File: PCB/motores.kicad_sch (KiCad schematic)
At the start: 30 parts, among them IC2 IR2175STRPBF, J10 Conn_01x03, J11 Conn_01x03, J12 motor_dc, J9 motor_lineal, K1 G6E, K2 G6E, K3 G6E, K4 G6E, Q1 AO3401A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

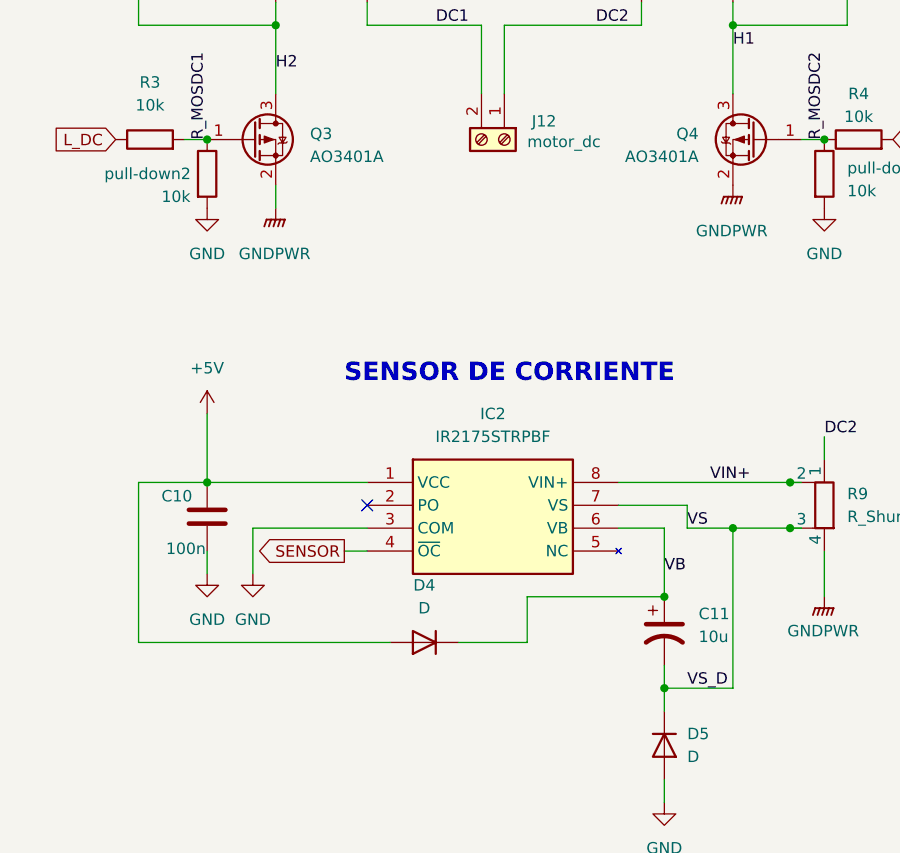
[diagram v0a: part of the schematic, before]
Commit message: Fixed labels and ERC errors
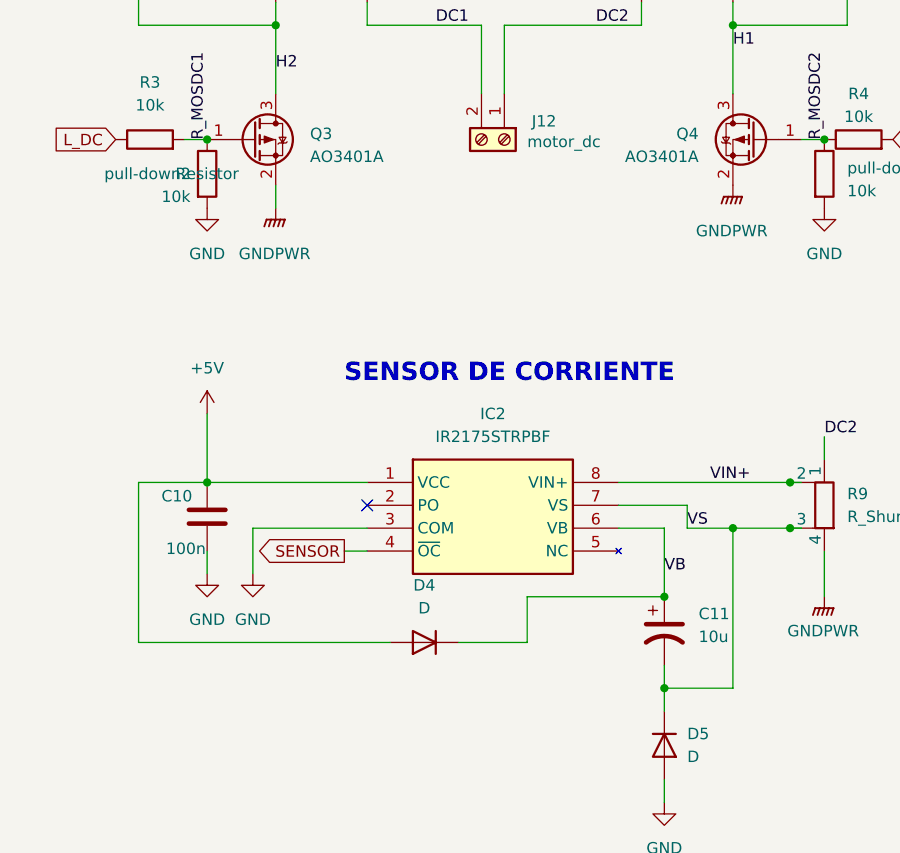
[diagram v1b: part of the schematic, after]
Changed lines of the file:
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@@
 	(wire
 		(pts
-			(xy 175.26 124.46) (xy 193.04 124.46)
-		)
-		(stroke
-			(width 0)
-			(type default)
-		)
-	)
-	(wire
-		(pts
 			(xy 50.8 60.96) (xy 63.5 60.96)
 		)
@@
 	(wire
 		(pts
+			(xy 175.26 124.46) (xy 193.04 124.46)
+		)
+		(stroke
+			(width 0)
+			(type default)
+		)
+	)
+	(wire
+		(pts
 			(xy 208.28 73.66) (xy 208.28 81.28)
 		)
@@
 		)
 	)
-	(label "VS_D"
-		(at 228.6 147.32 0)
-		(effects
-			(font
-				(size 1.27 1.27)
-			)
-			(justify left bottom)
-		)
-	)
 	(global_label "L_DC"
 		(shape input)
@@
 	)
 	(symbol
-		(lib_name "GND_1")
 		(lib_id "power:GND")
 		(at 66.04 142.24 0)
@@
 			)
 		)
-		(property "Description" ""
+		(property "Description" "-4.0A Id, -30V Vds, P-Channel MOSFET, SOT-23"
 			(at 236.22 86.36 0)
 			(effects
@@
 					(size 1.27 1.27)
 				)
+				(hide yes)
 			)
 		)
@@
 			)
 		)
-		(property "Description" ""
+		(property "Description" "Omron Subminiature Sensitive SPDT Signal Switching Relay, Single-Side Stable"
 			(at 109.22 73.66 0)
 			(effects
@@
 					(size 1.27 1.27)
 				)
+				(hide yes)
 			)
 		)
@@
 			)
 		)
-		(property "Description" ""
+		(property "Description" "Omron Subminiature Sensitive SPDT Signal Switching Relay, Single-Side Stable"
 			(at 68.58 73.66 0)
 			(effects
@@
 					(size 1.27 1.27)
 				)
+				(hide yes)
 			)
 		)
@@
 			)
 		)
-		(property "Description" ""
+		(property "Description" "Power symbol creates a global label with name \"GNDPWR\" , global ground"
 			(at 114.3 99.06 0)
 			(effects
@@
 					(size 1.27 1.27)
 				)
+				(hide yes)
 			)
 		)
@@
 			)
 		)
-		(property "Description" ""
+		(property "Description" "Resistor"
 			(at 49.53 91.44 0)
 			(effects
@@
 					(size 1.27 1.27)
 				)
+				(hide yes)
 			)
 		)
@@
 			)
 		)
-		(property "Description" ""
+		(property "Description" "Power symbol creates a global label with name \"GND\" , ground"
 			(at 121.92 101.6 0)
 			(effects
@@
 					(size 1.27 1.27)
 				)
+				(hide yes)
 			)
 		)
@@
 	)
 	(symbol
-		(lib_name "GNDPWR_1")
 		(lib_id "power:GNDPWR")
 		(at 243.84 137.16 0)
@@
 	)
 	(symbol
-		(lib_name "+12V_1")
 		(lib_id "power:+12V")
 		(at 88.9 58.42 0)
@@
 			)
 		)
-		(property "Description" ""
-			(at 63.5 99.06 0)
+		(property "Description" "Power symbol creates a global label with name \"GNDPWR\" , global ground"
+			(at 20.32 99.06 0)
 			(effects
 				(font
 					(size 1.27 1.27)
 				)
+				(hide yes)
 			)
 		)
@@
 			)
 		)
-		(property "Description" ""
+		(property "Description" "Resistor"
 			(at 121.92 97.79 0)
 			(effects
@@
 					(size 1.27 1.27)
 				)
+				(hide yes)
 			)
 		)
@@
 			)
 		)
-		(property "Description" ""
+		(property "Description" "Power symbol creates a global label with name \"GNDPWR\" , global ground"
 			(at 228.6 50.8 0)
 			(effects
@@
 					(size 1.27 1.27)
 				)
+				(hide yes)
 			)
 		)
@@
 	)
 	(symbol
-		(lib_name "GND_2")
 		(lib_id "power:GND")
 		(at 226.06 160.02 0)
@@
 			)
 		)
-		(property "Description" ""
+		(property "Description" "Resistor"
 			(at 243.84 90.17 0)
 			(effects
@@
 					(size 1.27 1.27)
 				)
+				(hide yes)
 			)
 		)
@@
 			)
 		)
-		(property "Description" ""
+		(property "Description" "Power symbol creates a global label with name \"+12V\""
 			(at 208.28 45.72 0)
 			(effects
@@
 					(size 1.27 1.27)
 				)
+				(hide yes)
 			)
 		)
@@
 			)
 		)
-		(property "Description" ""
+		(property "Description" "Resistor"
 			(at 175.26 90.17 0)
 			(effects
@@
 			)
 		)
-		(property "Description" ""
+		(property "Description" "Power symbol creates a global label with name \"GNDPWR\" , global ground"
 			(at 233.68 91.44 0)
 			(effects
@@
 					(size 1.27 1.27)
 				)
+				(hide yes)
 			)
 		)
@@
 			)
 		)
-		(property "Description" ""
+		(property "Description" "Power symbol creates a global label with name \"GNDPWR\" , global ground"
 			(at 182.88 93.98 0)
 			(effects
@@
 					(size 1.27 1.27)
 				)
+				(hide yes)
 			)
 		)
@@
 			)
 		)
-		(property "Description" ""
+		(property "Description" "Power symbol creates a global label with name \"GND\" , ground"
 			(at 175.26 93.98 0)
 			(effects
@@
 					(size 1.27 1.27)
 				)
+				(hide yes)
 			)
 		)
@@
 	)
 	(symbol
-		(lib_name "GND_1")
 		(lib_id "power:GND")
 		(at 92.71 142.24 0)
@@
 	)
 	(symbol
-		(lib_name "GND_3")
 		(lib_id "power:GND")
 		(at 175.26 134.62 0)
@@
 			)
 		)
-		(property "Description" ""
+		(property "Description" "Power symbol creates a global label with name \"GND\" , ground"
 			(at 243.84 93.98 0)
 			(effects
@@
 					(size 1.27 1.27)
 				)
+				(hide yes)
 			)
 		)
@@
 			)
 		)
-		(property "Description" ""
+		(property "Description" "Resistor"
 			(at 55.88 95.25 0)
 			(effects
@@
 					(size 1.27 1.27)
 				)
+				(hide yes)
 			)
 		)
@@
 	)
 	(symbol
-		(lib_name "GND_2")
 		(lib_id "power:GND")
 		(at 180.34 134.62 0)
@@
 	)
 	(symbol
-		(lib_name "GNDPWR_2")
 		(lib_id "power:GNDPWR")
 		(at 68.58 63.5 0)
@@
 		(on_board yes)
 		(dnp no)
-		(fields_autoplaced yes)
 		(property "Reference" "Q1"
 			(at 67.31 90.805 0)
@@
 			)
 		)
-		(property "Description" ""
-			(at 60.96 91.44 0)
+		(property "Description" "-4.0A Id, -30V Vds, P-Channel MOSFET, SOT-23"
+			(at 45.72 104.14 0)
 			(effects
 				(font
 					(size 1.27 1.27)
 				)
+				(hide yes)
 			)
 		)
@@
 			)
 		)
-		(property "Description" ""
+		(property "Description" "-4.0A Id, -30V Vds, P-Channel MOSFET, SOT-23"
 			(at 116.84 93.98 0)
 			(effects
@@
 					(size 1.27 1.27)
 				)
+				(hide yes)
 			)
 		)
@@
 			)
 		)
-		(property "Description" ""
+		(property "Description" "Omron Subminiature Sensitive SPDT Signal Switching Relay, Single-Side Stable"
 			(at 187.96 63.5 0)
 			(effects
@@
 					(size 1.27 1.27)
 				)
+				(hide yes)
 			)
 		)
@@
 			)
 		)
-		(property "Description" ""
+		(property "Description" "Power symbol creates a global label with name \"GNDPWR\" , global ground"
 			(at 187.96 48.26 0)
 			(effects
@@
 					(size 1.27 1.27)
 				)
+				(hide yes)
 			)
 		)
@@
 			)
 		)
-		(property "Description" ""
+		(property "Description" "Resistor"
 			(at 128.27 93.98 0)
 			(effects
@@
 					(size 1.27 1.27)
 				)
+				(hide yes)
 			)
 		)
@@
 	)
 	(symbol
-		(lib_name "GNDPWR_2")
 		(lib_id "power:GNDPWR")
 		(at 109.22 63.5 0)
@@
 			)
 		)
-		(property "Description" ""
+		(property "Description" "Omron Subminiature Sensitive SPDT Signal Switching Relay, Single-Side Stable"
 			(at 228.6 63.5 0)
 			(effects
@@
 					(size 1.27 1.27)
 				)
+				(hide yes)
 			)
 		)
@@
 			)
 		)
-		(property "Description" ""
+		(property "Description" "-4.0A Id, -30V Vds, P-Channel MOSFET, SOT-23"
 			(at 180.34 86.36 0)
 			(effects
@@
 					(size 1.27 1.27)
 				)
+				(hide yes)
 			)
 		)
@@
 			)
 		)
-		(property "Description" ""
+		(property "Description" "Power symbol creates a global label with name \"GND\" , ground"
 			(at 55.88 99.06 0)
 			(effects
@@
 					(size 1.27 1.27)
 				)
+				(hide yes)
 			)
 		)
@@
 			)
 		)
-		(property "Description" ""
+		(property "Description" "Resistor"
 			(at 247.65 86.36 0)
 			(effects
@@
 					(size 1.27 1.27)
 				)
+				(hide yes)
 			)
 		)

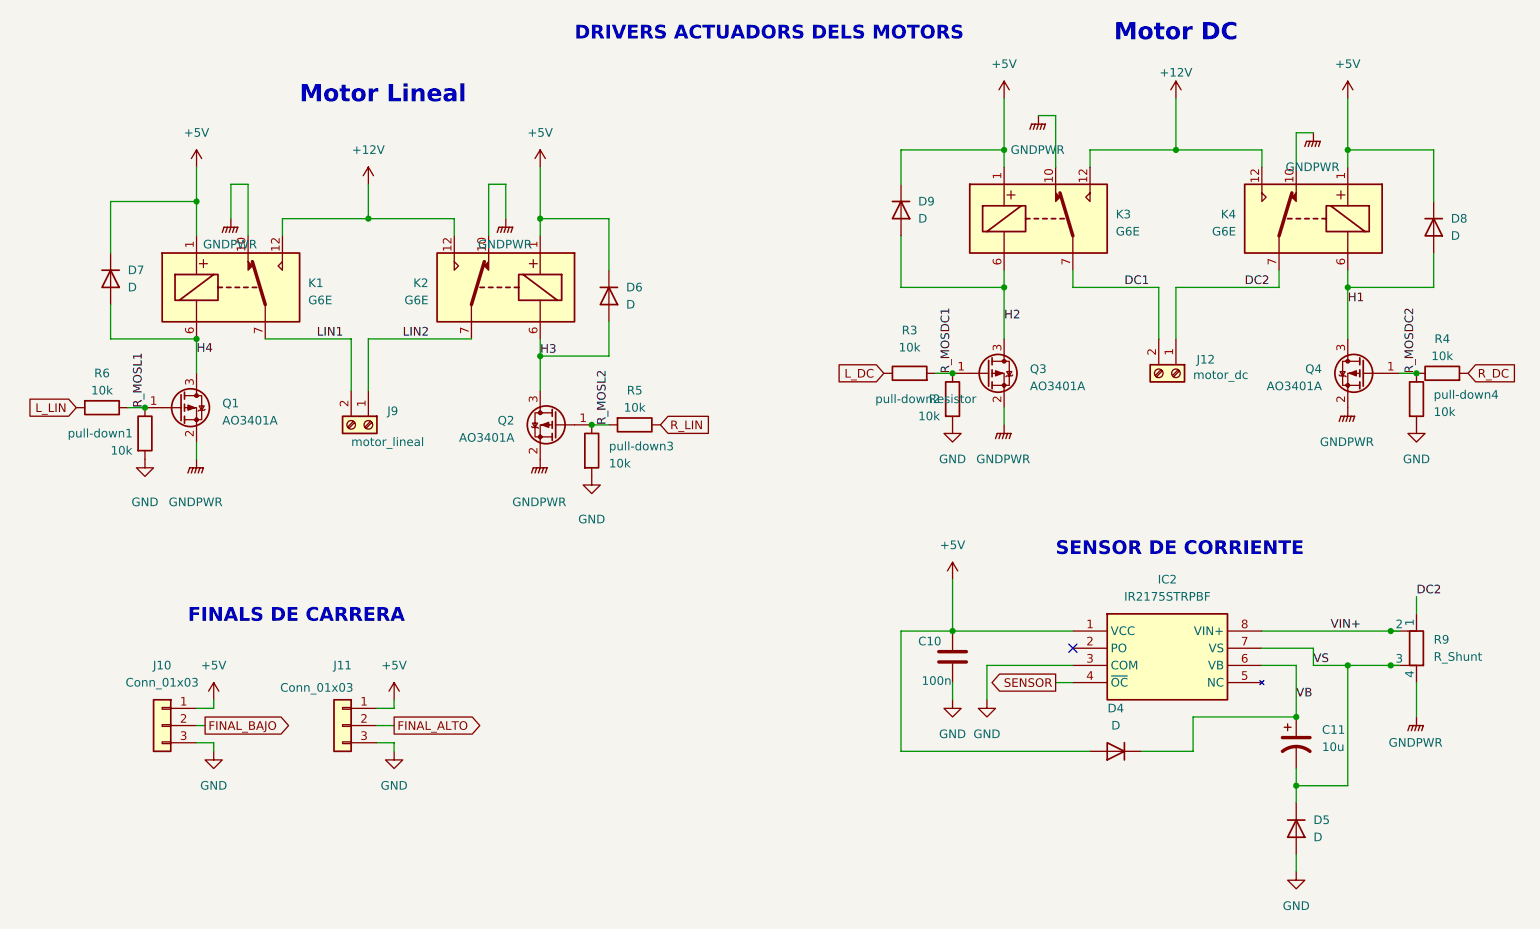
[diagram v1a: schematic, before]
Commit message: cambio de terminales tipo screw, final de carrera
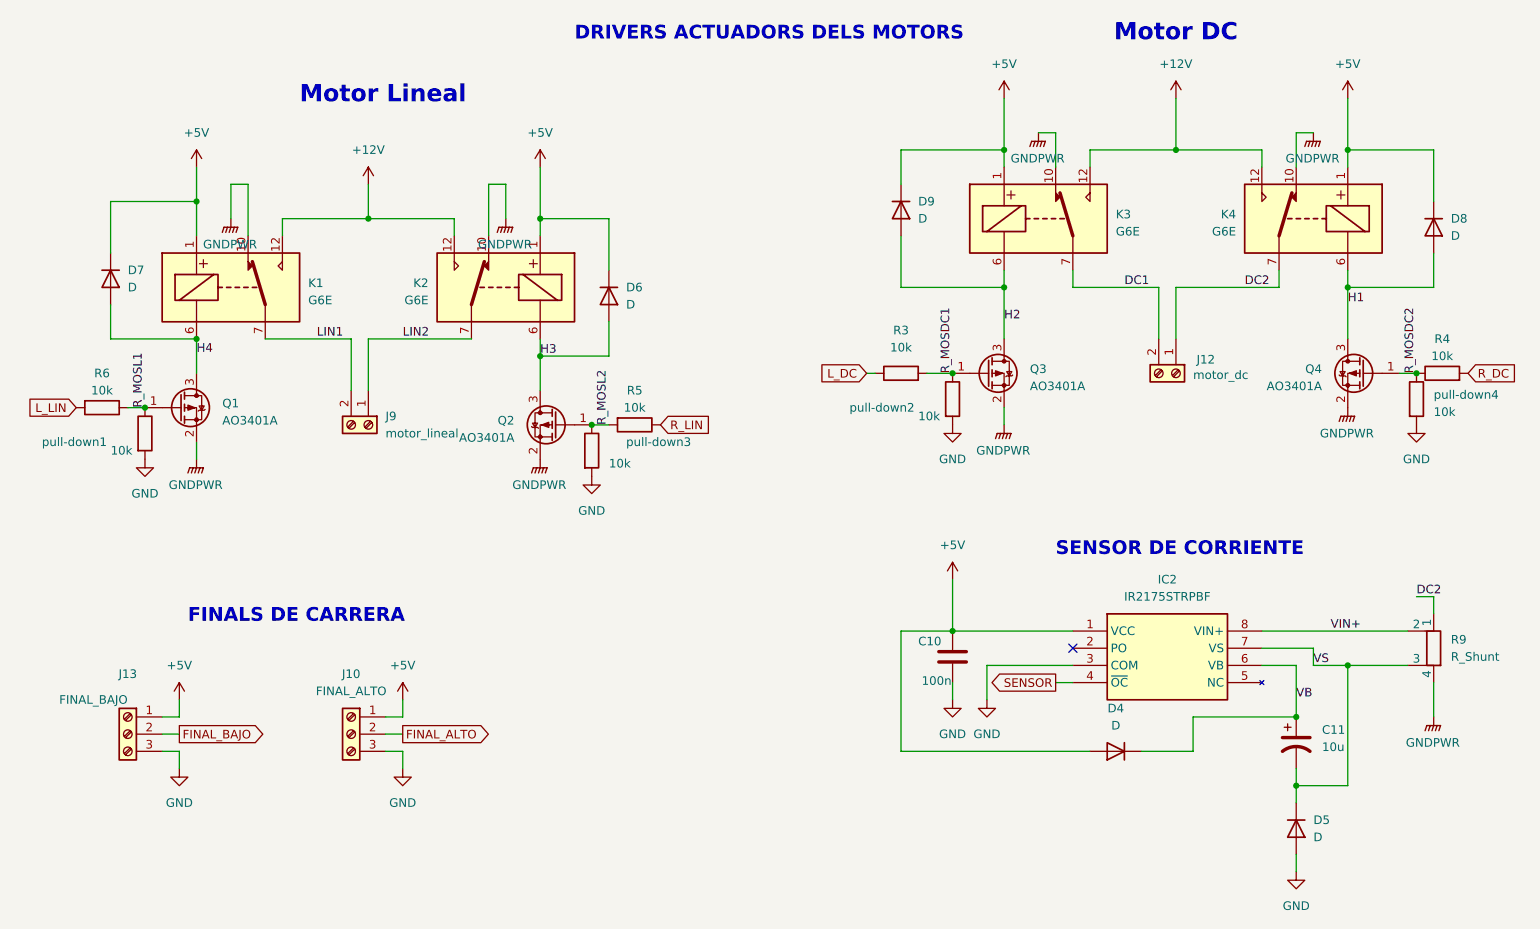
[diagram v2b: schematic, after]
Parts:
- removed J10, J11: Conn_01x03, Connector_PinHeader_2.54mm:PinHeader_1x03_P2.54mm_Vertical, symbol Connector_Generic:Conn_01x03
- added J10: FINAL_ALTO, TerminalBlock_Phoenix:TerminalBlock_Phoenix_MKDS-3-3-5.08_1x03_P5.08mm_Horizontal, symbol Connector:Screw_Terminal_01x03
- added J13: FINAL_BAJO, TerminalBlock_Phoenix:TerminalBlock_Phoenix_MKDS-3-3-5.08_1x03_P5.08mm_Horizontal, symbol Connector:Screw_Terminal_01x03
- J12, J9: footprint TerminalBlock_Phoenix:TerminalBlock_Phoenix_MPT-0,5-2-2.54_1x02_P2.54mm_Horizontal -> TerminalBlock_Phoenix:TerminalBlock_Phoenix_MKDS-3-2-5.08_1x02_P5.08mm_Horizontal
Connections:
- net +5V: now also J10.1 (Pin_1), J13.1 (Pin_1)
- net FINAL_ALTO: now also J10.2 (Pin_2)
- net FINAL_BAJO: now also J13.2 (Pin_2)
- net GND: now also J10.3 (Pin_3), J13.3 (Pin_3)
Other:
- moved on the sheet: R3, R9

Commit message: Update PCB
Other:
- note added: "DRIVERS ACTUADORES DE LOS MOTORS"
- note added: "FINALES DE CARRERA"
- note removed: "DRIVERS ACTUADORS DELS MOTORS"
- note removed: "FINALS DE CARRERA"
- title: (none) -> Motores
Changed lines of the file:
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@@
 	(generator_version "9.0")
 	(paper "A4")
-	(text "FINALS DE CARRERA\n"
+	(title_block
+		(title "Motores")
+		(rev "4/4")
+	)
+	(text "FINALES DE CARRERA\n"
 		(exclude_from_sim no)
 		(at 62.23 123.444 0)
@@
 		)
 	)
-	(text "DRIVERS ACTUADORS DELS MOTORS\n\n"
+	(text "DRIVERS ACTUADORES DE LOS MOTORS\n\n"
 		(exclude_from_sim no)
 		(at 119.38 40.64 0)
